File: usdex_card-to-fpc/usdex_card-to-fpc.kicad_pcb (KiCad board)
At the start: 6 copper layers, 11 x 15 mm, 2 parts, among them J1 Micro_SDex_PCB, J2 Conn_01x16_Socket

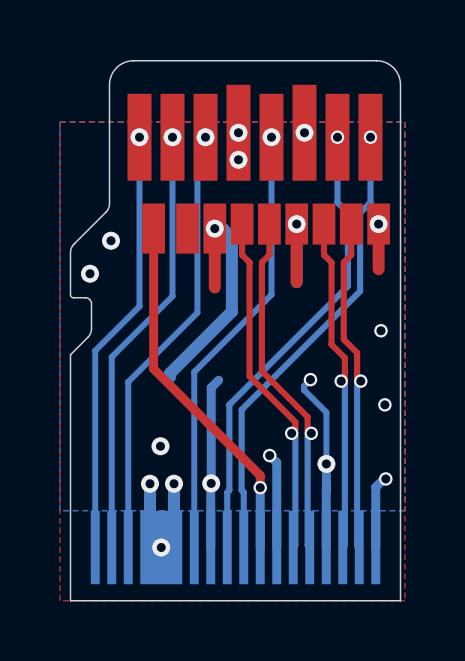
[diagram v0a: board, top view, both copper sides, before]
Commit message: add fillets and skew tuning
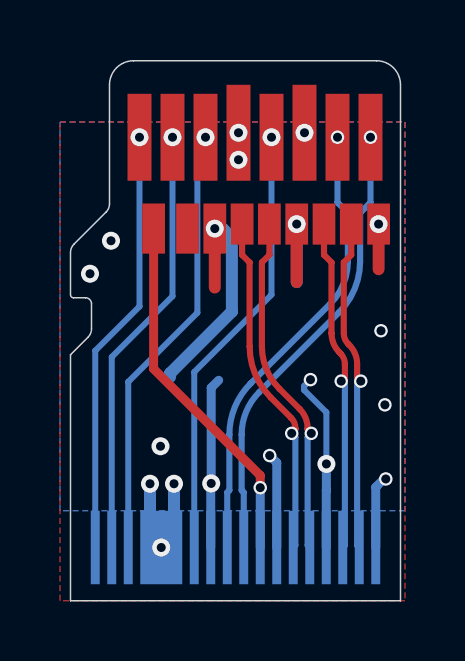
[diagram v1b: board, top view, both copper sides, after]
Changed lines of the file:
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@@
 	)
 	(segment
-		(start 1.345783 12.044589)
-		(end -0.179216 10.51959)
+		(start 1.199336 11.898142)
+		(end 0.526197 11.225003)
 		(width 0.205232)
 		(layer "F.Cu")
@@
 	(segment
 		(start 1.345783 12.297617)
-		(end 1.345783 12.044589)
+		(end 1.345783 12.251696)
 		(width 0.205232)
 		(layer "F.Cu")
@@
 	)
 	(segment
-		(start -0.179216 10.51959)
+		(start -0.179216 9.521985)
 		(end -0.179216 6.723285)
 		(width 0.205232)
@@
 		(drill 0.3)
 		(layers "F.Cu" "B.Cu")
+		(net 1)
+	)
+	(arc
+		(start 1.345783 12.251696)
+		(mid 1.307723 12.060354)
+		(end 1.199336 11.898142)
+		(width 0.205232)
+		(layer "F.Cu")
+		(net 1)
+	)
+	(arc
+		(start -0.179216 9.521985)
+		(mid 0.004115 10.443652)
+		(end 0.526197 11.225003)
+		(width 0.205232)
+		(layer "F.Cu")
 		(net 1)
 	)
@@
 	(segment
 		(start 1.754217 12.297617)
-		(end 1.754217 11.875411)
+		(end 1.754217 12.251696)
 		(width 0.205232)
 		(layer "F.Cu")
@@
 	)
 	(segment
-		(start 0.229216 10.35041)
+		(start 0.229216 9.521983)
 		(end 0.229216 6.723285)
 		(width 0.205232)
@@
 	)
 	(segment
-		(start 1.754217 11.875411)
-		(end 0.229216 10.35041)
+		(start 1.488143 11.609337)
+		(end 0.815002 10.936196)
 		(width 0.205232)
 		(layer "F.Cu")
@@
 		(net 2)
 	)
+	(arc
+		(start 0.815002 10.936196)
+		(mid 0.381457 10.28735)
+		(end 0.229216 9.521983)
+		(width 0.205232)
+		(layer "F.Cu")
+		(net 2)
+	)
+	(arc
+		(start 1.488143 11.609337)
+		(mid 1.685067 11.904054)
+		(end 1.754217 12.251696)
+		(width 0.205232)
+		(layer "F.Cu")
+		(net 2)
+	)
 	(segment
 		(start 1.825 16.225)
@@
 	)
 	(segment
-		(start 3.095784 7.51541)
+		(start 3.095784 6.686983)
 		(end 3.095784 5.070785)
 		(width 0.205232)
@@
 	)
 	(segment
-		(start -0.854216 11.46541)
-		(end 3.095784 7.51541)
+		(start -0.148802 10.759996)
+		(end 2.509998 8.101196)
 		(width 0.205232)
 		(layer "B.Cu")
@@
 	(segment
 		(start -0.854216 14.316715)
-		(end -0.854216 11.46541)
+		(end -0.854216 12.463015)
+		(width 0.205232)
+		(layer "B.Cu")
+		(net 4)
+	)
+	(arc
+		(start -0.854216 12.463015)
+		(mid -0.670885 11.541348)
+		(end -0.148802 10.759996)
+		(width 0.205232)
+		(layer "B.Cu")
+		(net 4)
+	)
+	(arc
+		(start 2.509998 8.101196)
+		(mid 2.943543 7.45235)
+		(end 3.095784 6.686983)
 		(width 0.205232)
 		(layer "B.Cu")
@@
 	)
 	(segment
-		(start 3.404217 9.735411)
-		(end 2.959216 9.29041)
+		(start 3.138143 9.469337)
+		(end 3.105662 9.436856)
 		(width 0.205232)
 		(layer "F.Cu")
@@
 	)
 	(segment
-		(start 2.959216 9.29041)
+		(start 2.959216 9.083303)
 		(end 2.959216 6.723285)
 		(width 0.205232)
@@
 	(segment
 		(start 3.404217 10.557617)
-		(end 3.404217 9.735411)
+		(end 3.404217 10.111696)
 		(width 0.205232)
 		(layer "F.Cu")
@@
 		(drill 0.3)
 		(layers "F.Cu" "B.Cu")
+		(net 9)
+	)
+	(arc
+		(start 2.959216 9.083303)
+		(mid 2.997276 9.274644)
+		(end 3.105662 9.436856)
+		(width 0.205232)
+		(layer "F.Cu")
+		(net 9)
+	)
+	(arc
+		(start 3.138143 9.469337)
+		(mid 3.335067 9.764054)
+		(end 3.404217 10.111696)
+		(width 0.205232)
+		(layer "F.Cu")
 		(net 9)
 	)
@@
 	(segment
 		(start 2.995783 10.557617)
-		(end 2.995783 9.904589)
+		(end 2.995783 10.111696)
 		(width 0.205232)
 		(layer "F.Cu")
@@
 	)
 	(segment
-		(start 2.995783 9.904589)
-		(end 2.550784 9.45959)
+		(start 2.849336 9.758142)
+		(end 2.816857 9.725663)
 		(width 0.205232)
 		(layer "F.Cu")
@@
 	)
 	(segment
-		(start 2.550784 9.45959)
+		(start 2.550784 9.083305)
 		(end 2.550784 6.723285)
 		(width 0.205232)
@@
 		(drill 0.3)
 		(layers "F.Cu" "B.Cu")
+		(net 13)
+	)
+	(arc
+		(start 2.995783 10.111696)
+		(mid 2.957723 9.920354)
+		(end 2.849336 9.758142)
+		(width 0.205232)
+		(layer "F.Cu")
+		(net 13)
+	)
+	(arc
+		(start 2.816857 9.725663)
+		(mid 2.619934 9.430947)
+		(end 2.550784 9.083305)
+		(width 0.205232)
+		(layer "F.Cu")
 		(net 13)
 	)
@@
 	)
 	(segment
-		(start -0.445784 11.63459)
-		(end 3.504216 7.68459)
+		(start 0.140003 11.048803)
+		(end 2.798803 8.390003)
 		(width 0.205232)
 		(layer "B.Cu")
@@
 	(segment
 		(start -0.445784 14.316715)
-		(end -0.445784 11.63459)
+		(end -0.445784 12.463017)
 		(width 0.205232)
 		(layer "B.Cu")
@@
 	)
 	(segment
-		(start 3.504216 7.68459)
+		(start 3.504216 6.686985)
 		(end 3.504216 5.070785)
 		(width 0.205232)
@@
 		(width 0.205232)
 		(layer "B.Cu")
+		(net 14)
+	)
+	(arc
+		(start 3.504216 6.686985)
+		(mid 3.320885 7.608652)
+		(end 2.798803 8.390003)
+		(width 0.205232)
+		(layer "B.Cu")
+		(net 14)
+	)
+	(arc
+		(start 0.140003 11.048803)
+		(mid -0.293543 11.69765)
+		(end -0.445784 12.463017)
+		(width 0.205232)
+		(layer "B.Cu")
